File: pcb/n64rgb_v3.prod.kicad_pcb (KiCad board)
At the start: 2 copper layers, 160.3 x 25.5 mm, 60 parts, among them J1 Conn_01x01_Male, J10 Conn_01x01_Male, J2 Conn_01x01_Male, J3 Conn_01x01_Male, J4 Conn_01x01_Male, J5 Conn_01x01_Male, J6 Conn_01x01_Male, J7 OS202011MS2QS1, J8 Conn_01x01_Male, J9 Conn_01x01_Male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

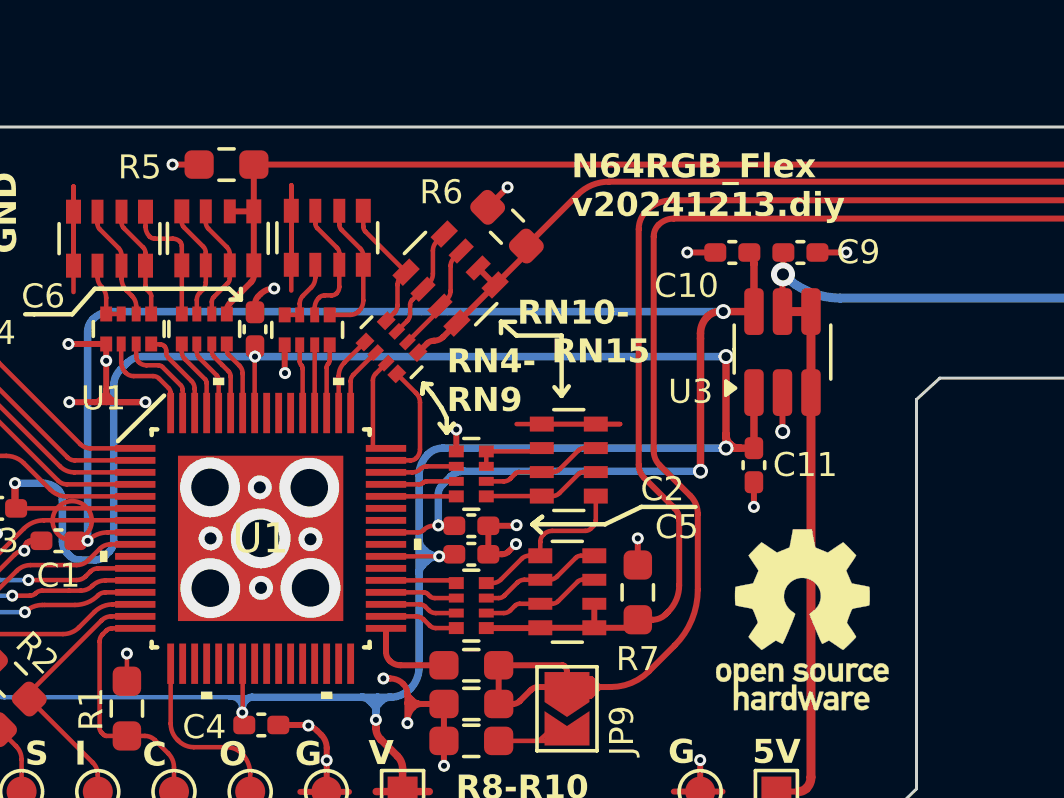
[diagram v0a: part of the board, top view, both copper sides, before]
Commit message: Update PCB for use with 5M80ZE64 CPLD
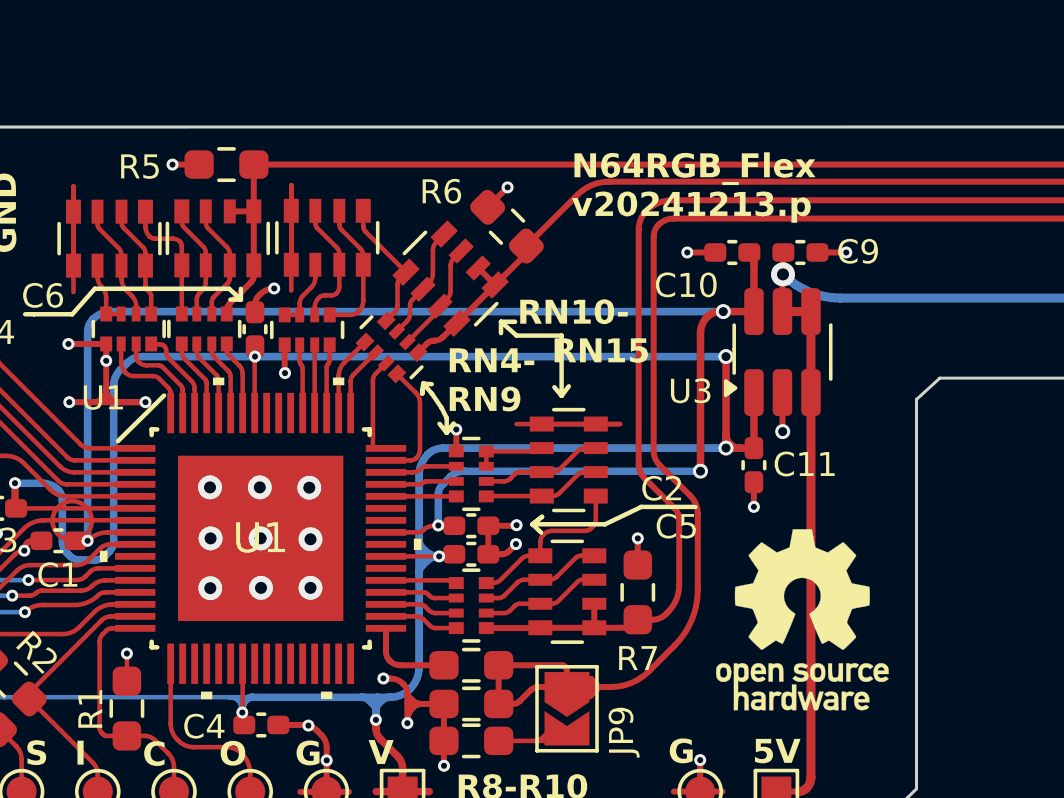
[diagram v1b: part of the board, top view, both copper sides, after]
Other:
- board text added: "N64RGB_Flex v20241213.p"
- board text removed: "N64RGB_Flex v20241213.diy"
